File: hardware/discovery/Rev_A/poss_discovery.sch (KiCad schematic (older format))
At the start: 56 parts, among them J1 HEADER_2, J2 HEADER_25x2, J3 HEADER_25x2, J5 HEADER_2, SW1 SW_PUSH, SW10 SW_PUSH, SW11 SW_PUSH, SW12 SW_PUSH, SW13 SW_PUSH, SW14 SW_PUSH, SW15 SW_PUSH, SW16 SW_PUSH, SW17 SW_PUSH, SW18 SW_PUSH, SW19 SW_PUSH, SW2 SW_PUSH, SW20 SW_PUSH, SW21 SW_PUSH, SW22 SW_PUSH, SW3 SW_PUSH, SW4 SW_PUSH, SW5 SW_PUSH, SW6 SW_PUSH, SW7 SW_PUSH, SW8 SW_PUSH, SW9 SW_PUSH

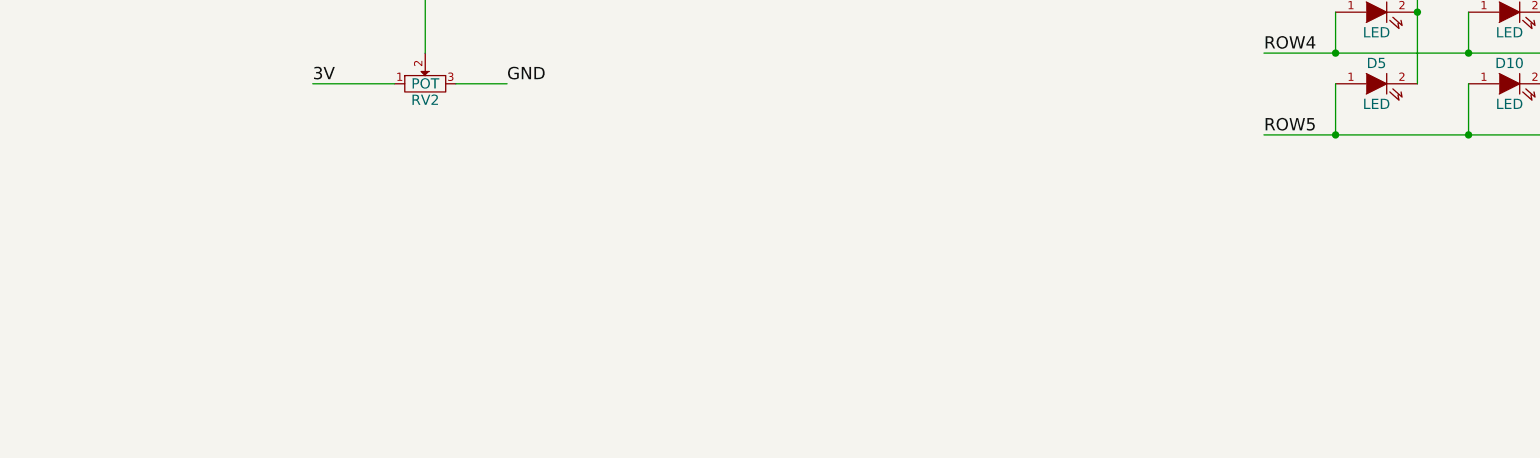
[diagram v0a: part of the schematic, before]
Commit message: Add known problems to the  RevA schematics
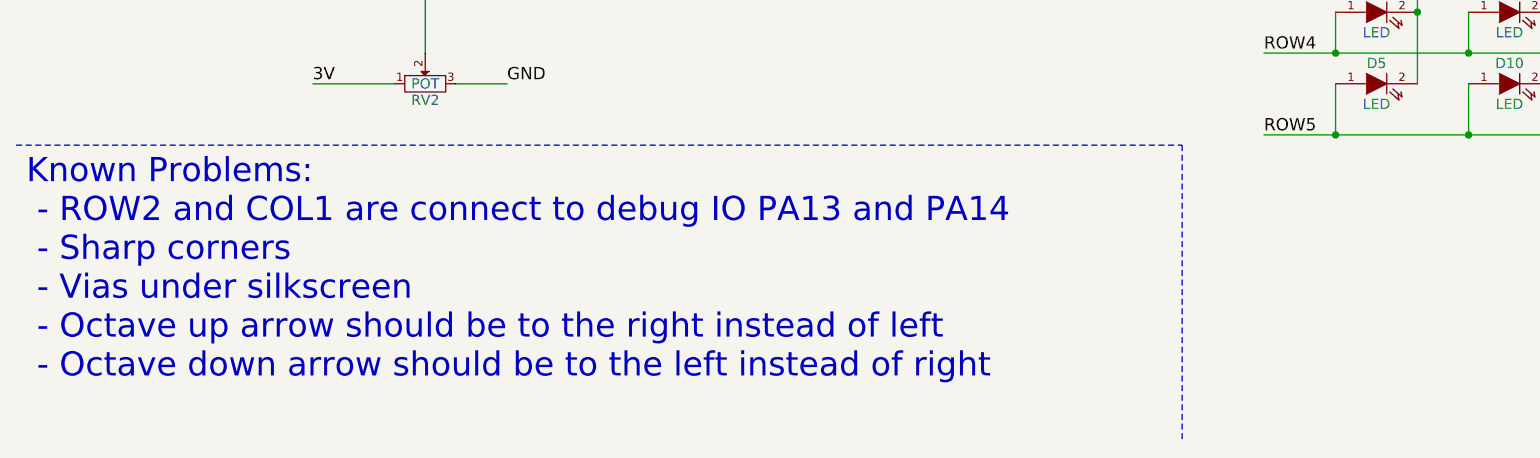
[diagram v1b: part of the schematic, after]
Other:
- note added: "Known Problems:\n - ROW2 and COL1 are connect to debug IO PA13 and PA14\n - Sharp corners\n - Vias under silkscreen\n - Octave up arrow should be to the right instead of left\n - Octave down arrow should be to the left instead of right"
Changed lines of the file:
@@
 encoding utf-8
 Sheet 1 1
-Title ""
+Title "Pocket Open Source Synthesizer"
 Date ""
-Rev ""
-Comp ""
+Rev "A"
+Comp "Fabien Chouteau"
 Comment1 ""
 Comment2 ""
@@
 Text Label 1550 2900 0    60   ~ 0
 POT1
+Text Notes 550  7450 0    118  ~ 0
+Known Problems:\n - ROW2 and COL1 are connect to debug IO PA13 and PA14\n - Sharp corners\n - Vias under silkscreen\n - Octave up arrow should be to the right instead of left\n - Octave down arrow should be to the left instead of right
+Wire Notes Line
+	500  6300 6200 6300
+Wire Notes Line
+	6200 6300 6200 7750
 $EndSCHEMATC
